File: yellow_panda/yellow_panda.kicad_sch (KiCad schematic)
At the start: 10 parts, among them P1 USB_C_Plug_USB2.0, P2 USB_C_Plug_USB2.0, U3 LT1963AxST-3.3, U4 LT1963AxST-3.3

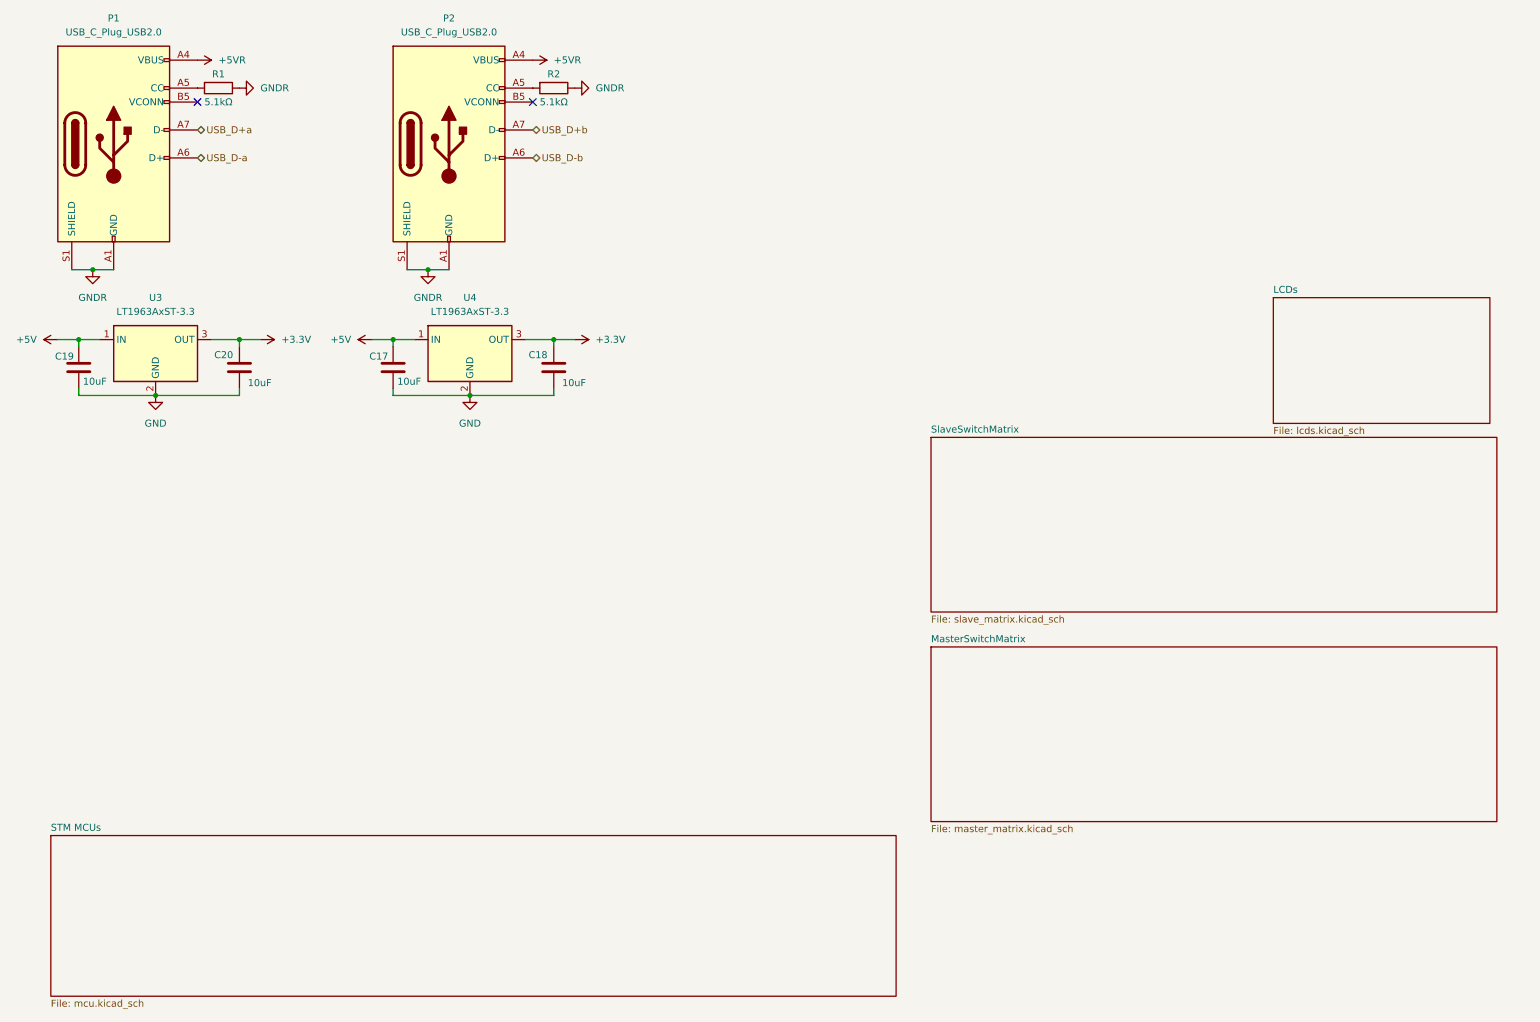
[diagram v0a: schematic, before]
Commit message: Everything is in place now
Swap STM MCU, Correct Switches,
add diodes, caps and resistors
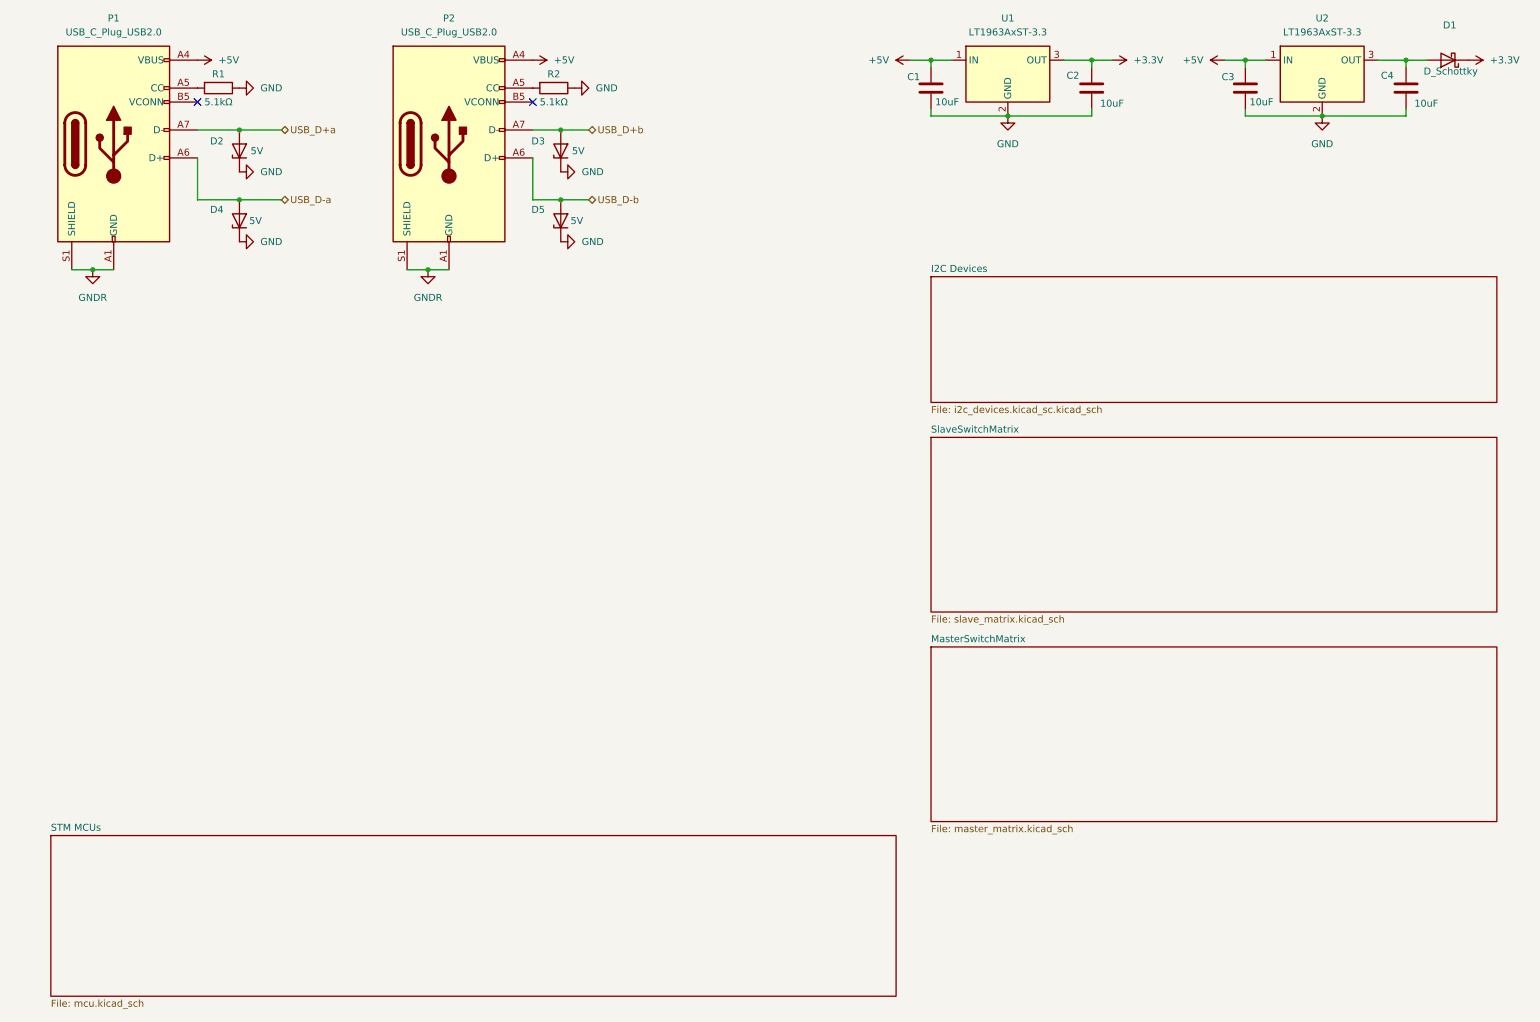
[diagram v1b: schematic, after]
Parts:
- added D1: D_Schottky, PCM_JLCPCB:D_SOT-23, symbol Device:D_Schottky
- added D2, D3, D4, D5: 5V, PCM_JLCPCB:D_SOT-23, symbol Diode:PESD5V0L1UL
- C1: renamed from C19; footprint (none) -> Capacitor_SMD:C_1206_3216Metric_Pad1.33x1.80mm_HandSolder
- C2: renamed from C20; footprint (none) -> Capacitor_SMD:C_1206_3216Metric_Pad1.33x1.80mm_HandSolder
- C3: renamed from C17; footprint (none) -> Capacitor_SMD:C_1206_3216Metric_Pad1.33x1.80mm_HandSolder
- C4: renamed from C18; footprint (none) -> Capacitor_SMD:C_1206_3216Metric_Pad1.33x1.80mm_HandSolder
- P1, P2: footprint usb-c:CONN16_USB4085-GF-A_GCT -> Custom Lib:USB_C_Receptacle_GCT_USB4110
- renumbered U3 to U1, U4 to U2
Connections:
- net +5VR is gone; now on net +5V: P1.A4 (VBUS), P1.A9 (VBUS), P1.B4 (VBUS), P1.B9 (VBUS), P2.A4 (VBUS), P2.A9 (VBUS), P2.B4 (VBUS), P2.B9 (VBUS)
- net +3.3V: now also D1.1 (K); no longer C4.1, U2.3 (OUT)
- net GND: now also R1.1, R2.1, D2.1 (K), D3.1 (K), D4.1 (K), D5.1 (K)
- net GNDR: no longer R1.1, R2.1
- net USB_D+a: now also D2.2 (A)
- net USB_D+b: now also D3.2 (A)
- net USB_D-a: now also D4.2 (A)
- net USB_D-b: now also D5.2 (A)
- new net: C4.1, D1.2 (A), U2.3 (OUT)
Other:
- sheet LCDs renamed I2C Devices
- sheet I2C Devices: file lcds.kicad_sch -> i2c_devices.kicad_sc.kicad_sch
- moved on the sheet: C1, C2, C3, C4, U1, U2

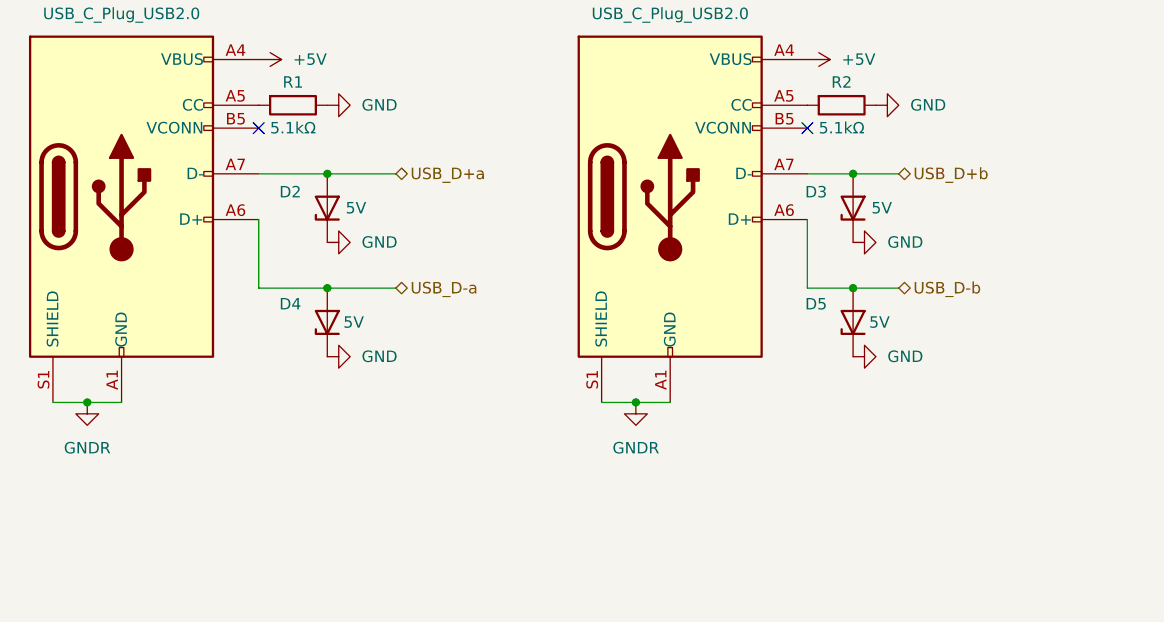
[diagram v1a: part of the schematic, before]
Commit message: Added some routing to power lines
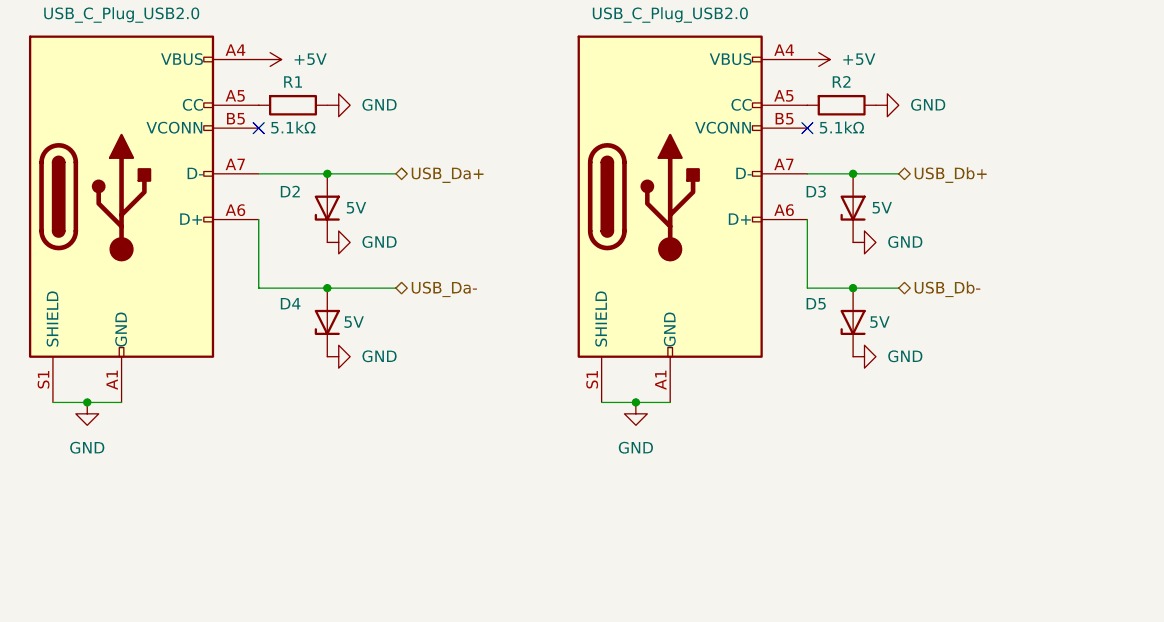
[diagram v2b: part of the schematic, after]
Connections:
- net GNDR is gone; now on net GND: P1.A1 (GND), P1.A12 (GND), P1.B1 (GND), P1.B12 (GND), P1.S1 (SHIELD), P2.A1 (GND), P2.A12 (GND), P2.B1 (GND), P2.B12 (GND), P2.S1 (SHIELD)
- net USB_D+a renamed USB_Da+
- net USB_D+b renamed USB_Db+
- net USB_D-a renamed USB_Da-
- net USB_D-b renamed USB_Db-

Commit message: rev0.1a - master half done
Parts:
- removed D2, D3, D4, D5: 5V, PCM_JLCPCB:D_SOT-23, symbol Diode:PESD5V0L1UL
- added C23, C24: 100nF, Capacitor_SMD:C_0201_0603Metric_Pad0.64x0.40mm_HandSolder, symbol Device:C
- added D2, D3: SMF5.0A, PCM_JLCPCB:D_SOD-123FL, symbol PCM_JLCPCB-Diodes:TVS-Uni,SMF5.0A
- added U5, U6: USBLC6-2SC6, Package_TO_SOT_SMD:SOT-23-6, symbol Power_Protection:USBLC6-2SC6
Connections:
- net +5V: now also C23.1, C24.1, D2.1, D3.1, U5.5 (VBUS), U6.5 (VBUS); no longer P1.A4 (VBUS), P1.A9 (VBUS), P1.B4 (VBUS), P1.B9 (VBUS), P2.A4 (VBUS), P2.A9 (VBUS), P2.B4 (VBUS), P2.B9 (VBUS)
- net GND: now also C23.2, C24.2, U5.2 (GND), U6.2 (GND)
- net USB_Db+: now also U6.1 (I/O1); no longer P2.A7 (D-)
- net USB_Db-: now also U6.6 (I/O1); no longer P2.A6 (D+)
- net USB_Da+: no longer names the net of P1.A7 (D-)
- net USB_Da+: now also U5.3 (I/O2)
- net USB_Da-: no longer names the net of P1.A6 (D+)
- net USB_Da-: now also U5.4 (I/O2)
- new net: P2.A7 (D-), U6.3 (I/O2)
- new net: P2.A6 (D+), U6.4 (I/O2)
- new net USBDa+: U5.1 (I/O1)
- new net USBDa-: U5.6 (I/O1)
- new net VBUSa: D2.2, P1.A4 (VBUS), P1.A9 (VBUS), P1.B4 (VBUS), P1.B9 (VBUS)
- new net VBUSb: D3.2, P2.A4 (VBUS), P2.A9 (VBUS), P2.B4 (VBUS), P2.B9 (VBUS)
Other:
- removed sheet I2C Devices
- added sheet Devices (devices.kicad_sc.kicad_sch)
- added sheet LED Sheet (MasterLed.kicad_sch)

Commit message: Finished the design
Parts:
- removed D1: D_Schottky, PCM_JLCPCB:D_SOT-23, symbol Device:D_Schottky
- added C26, C27: 100nF, Capacitor_SMD:C_0201_0603Metric_Pad0.64x0.40mm_HandSolder, symbol Device:C
- added R5: 330, Resistor_SMD:R_2512_6332Metric_Pad1.40x3.35mm_HandSolder, symbol Device:R
- added R6: 10k, Resistor_SMD:R_0402_1005Metric_Pad0.72x0.64mm_HandSolder, symbol Device:R
- added U9: TPS2115ADRBR, Custom Lib:DRB8_2P4X1P65, symbol power_selector:TPS2115ADRBR
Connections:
- net +3.3V: now also C4.1, U2.3 (OUT)
- net +5V: now also R6.1, U9.7 (OUT); no longer D3.1
- net GND: now also C26.1, C27.1, R5.2, U9.2 (D0), U9.3 (D1), U9.5 (GND), U9.9 (EPAD)
- net USB_Db+ renamed USBDb+
- net USB_Db- renamed USBDb-
- new net: R5.1, U9.4 (ILIM)
- new net: R6.2, U9.1 (STAT)
- new net VBUS MASTER HALF: C27.2, U9.6 (IN2)
- new net VBUS USB: C26.2, D3.1, U9.8 (IN1)
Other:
- sheet LED Sheet renamed LED Master Sheet
- added sheet LED Slave (SlaveLed.kicad_sch)
